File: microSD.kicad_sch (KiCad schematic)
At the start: 7 parts, among them J2 5027740891

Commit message: some cleanup
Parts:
- J2: MnfNumber (none) -> 5027740891
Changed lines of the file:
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@@
       (effects (font (size 1.27 1.27) italic) hide)
+    )
+    (property "MnfNumber" "5027740891" (at 151.765 76.2 0)
+      (effects (font (size 1.27 1.27)) hide)
     )
     (pin "1")

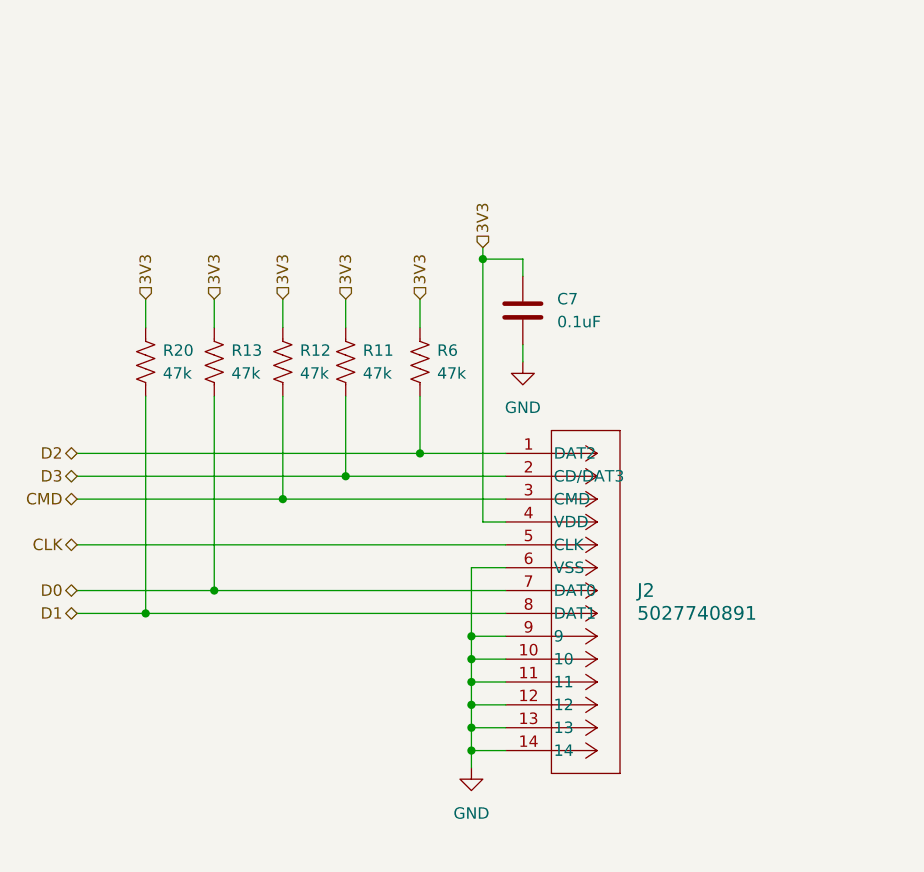
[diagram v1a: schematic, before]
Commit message: updated parts with those available on jlpcb
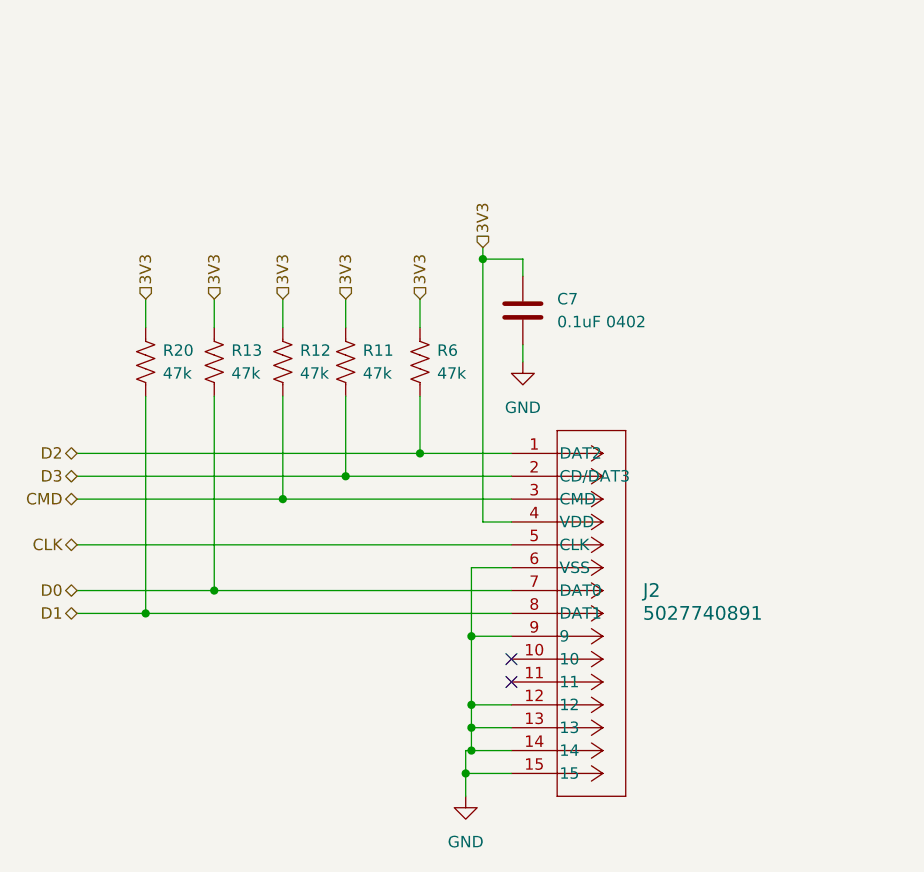
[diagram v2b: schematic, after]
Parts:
- C7: value 0.1uF -> 0.1uF 0402
- J2: footprint microSD:CONN_5027740891_MOL -> microSD2:CONN9_0185-02_GSW
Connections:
- net GND: now also J2.15; no longer J2.10, J2.11
- no-connect marks 0 -> 2
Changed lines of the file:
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@@
 (kicad_sch (version 20230121) (generator eeschema)
   (paper "A4")
-  (junction (at 147.955 101.6) (diameter 0) (color 0 0 0 0)
+  (junction (at 147.32 111.76) (diameter 0) (color 0 0 0 0)
   )
   (junction (at 142.24 76.2) (diameter 0) (color 0 0 0 0)
@@
   (junction (at 147.955 96.52) (diameter 0) (color 0 0 0 0)
   )
-  (junction (at 147.955 99.06) (diameter 0) (color 0 0 0 0)
-  )
+  (no_connect (at 152.4 99.06))
+  (no_connect (at 152.4 101.6))
   (wire (pts (xy 153.67 64.135) (xy 153.67 66.04))
     (stroke (width 0) (type default))
   )
+  (wire (pts (xy 147.32 111.76) (xy 152.4 111.76))
+    (stroke (width 0) (type default))
+  )
   (wire (pts (xy 104.14 76.2) (xy 142.24 76.2))
     (stroke (width 0) (type default))
@@
     (stroke (width 0) (type default))
   )
-  (wire (pts (xy 142.24 76.2) (xy 151.765 76.2))
+  (wire (pts (xy 142.24 76.2) (xy 152.4 76.2))
     (stroke (width 0) (type default))
   )
@@
     (stroke (width 0) (type default))
   )
-  (wire (pts (xy 127 81.28) (xy 151.765 81.28))
+  (wire (pts (xy 127 81.28) (xy 152.4 81.28))
     (stroke (width 0) (type default))
   )
@@
     (stroke (width 0) (type default))
   )
-  (wire (pts (xy 147.955 106.68) (xy 151.765 106.68))
-    (stroke (width 0) (type default))
-  )
-  (wire (pts (xy 147.955 111.125) (xy 147.955 109.22))
-    (stroke (width 0) (type default))
-  )
-  (wire (pts (xy 147.955 109.22) (xy 151.765 109.22))
+  (wire (pts (xy 147.955 106.68) (xy 152.4 106.68))
+    (stroke (width 0) (type default))
+  )
+  (wire (pts (xy 147.32 114.3) (xy 147.32 111.76))
+    (stroke (width 0) (type default))
+  )
+  (wire (pts (xy 147.955 109.22) (xy 152.4 109.22))
     (stroke (width 0) (type default))
   )
@@
     (stroke (width 0) (type default))
   )
-  (wire (pts (xy 147.955 101.6) (xy 147.955 99.06))
-    (stroke (width 0) (type default))
-  )
-  (wire (pts (xy 147.955 88.9) (xy 151.765 88.9))
-    (stroke (width 0) (type default))
-  )
-  (wire (pts (xy 133.985 78.74) (xy 151.765 78.74))
+  (wire (pts (xy 147.32 111.76) (xy 147.32 109.22))
+    (stroke (width 0) (type default))
+  )
+  (wire (pts (xy 147.955 88.9) (xy 152.4 88.9))
+    (stroke (width 0) (type default))
+  )
+  (wire (pts (xy 133.985 78.74) (xy 152.4 78.74))
     (stroke (width 0) (type default))
   )
@@
     (stroke (width 0) (type default))
   )
-  (wire (pts (xy 147.955 104.14) (xy 147.955 101.6))
-    (stroke (width 0) (type default))
-  )
   (wire (pts (xy 104.14 93.98) (xy 111.76 93.98))
     (stroke (width 0) (type default))
   )
-  (wire (pts (xy 111.76 93.98) (xy 151.765 93.98))
-    (stroke (width 0) (type default))
-  )
-  (wire (pts (xy 147.955 101.6) (xy 151.765 101.6))
+  (wire (pts (xy 111.76 93.98) (xy 152.4 93.98))
     (stroke (width 0) (type default))
   )
@@
     (stroke (width 0) (type default))
   )
-  (wire (pts (xy 147.955 104.14) (xy 151.765 104.14))
-    (stroke (width 0) (type default))
-  )
-  (wire (pts (xy 149.225 83.82) (xy 151.765 83.82))
+  (wire (pts (xy 147.955 104.14) (xy 152.4 104.14))
+    (stroke (width 0) (type default))
+  )
+  (wire (pts (xy 149.225 83.82) (xy 152.4 83.82))
     (stroke (width 0) (type default))
   )
@@
     (stroke (width 0) (type default))
   )
-  (wire (pts (xy 147.955 96.52) (xy 151.765 96.52))
-    (stroke (width 0) (type default))
-  )
-  (wire (pts (xy 147.955 99.06) (xy 151.765 99.06))
+  (wire (pts (xy 147.955 96.52) (xy 152.4 96.52))
+    (stroke (width 0) (type default))
+  )
+  (wire (pts (xy 147.32 109.22) (xy 147.955 109.22))
     (stroke (width 0) (type default))
   )
@@
     (stroke (width 0) (type default))
   )
-  (wire (pts (xy 119.38 91.44) (xy 151.765 91.44))
+  (wire (pts (xy 119.38 91.44) (xy 152.4 91.44))
     (stroke (width 0) (type default))
   )
@@
     (stroke (width 0) (type default))
   )
-  (wire (pts (xy 104.14 86.36) (xy 151.765 86.36))
+  (wire (pts (xy 104.14 86.36) (xy 152.4 86.36))
     (stroke (width 0) (type default))
   )
@@
     (stroke (width 0) (type default))
   )
-  (wire (pts (xy 147.955 99.06) (xy 147.955 96.52))
+  (wire (pts (xy 147.955 96.52) (xy 147.955 104.14))
     (stroke (width 0) (type default))
   )
@@
       (effects (font (size 1.27 1.27)) (justify left))
     )
-    (property "Value" "0.1uF" (at 157.48 61.595 0)
+    (property "Value" "0.1uF 0402" (at 157.48 61.595 0)
       (effects (font (size 1.27 1.27)) (justify left))
     )
@@
     )
   )
-  (symbol (lib_id "microSD:5027740891") (at 151.765 76.2 0) (unit 1)
-    (in_bom yes) (on_board yes) (dnp no) (fields_autoplaced)
-    (property "Reference" "J2" (at 166.37 91.44 0)
+  (symbol (lib_id "microSD:5027740891") (at 152.4 76.2 0) (unit 1)
+    (in_bom yes) (on_board yes) (dnp no) (fields_autoplaced)
+    (property "Reference" "J2" (at 167.005 91.44 0)
       (effects (font (size 1.524 1.524)) (justify left))
     )
-    (property "Value" "5027740891" (at 166.37 93.98 0)
+    (property "Value" "5027740891" (at 167.005 93.98 0)
       (effects (font (size 1.524 1.524)) (justify left))
     )
-    (property "Footprint" "microSD:CONN_5027740891_MOL" (at 151.765 76.2 0)
+    (property "Footprint" "microSD2:CONN9_0185-02_GSW" (at 152.4 76.2 0)
       (effects (font (size 1.27 1.27) italic) hide)
     )
-    (property "Datasheet" "5027740891" (at 151.765 76.2 0)
+    (property "Datasheet" "5027740891" (at 152.4 76.2 0)
       (effects (font (size 1.27 1.27) italic) hide)
     )
-    (property "MnfNumber" "5027740891" (at 151.765 76.2 0)
+    (property "MnfNumber" "5027740891" (at 152.4 76.2 0)
       (effects (font (size 1.27 1.27)) hide)
     )
@@
     (pin "13")
     (pin "14")
+    (pin "15")
     (pin "2")
     (pin "3")
@@
     )
   )
-  (symbol (lib_id "power:GND") (at 147.955 111.125 0) (unit 1)
-    (in_bom yes) (on_board yes) (dnp no) (fields_autoplaced)
-    (property "Reference" "#PWR017" (at 147.955 117.475 0)
-      (effects (font (size 1.27 1.27)) hide)
-    )
-    (property "Value" "GND" (at 147.955 116.205 0)
+  (symbol (lib_id "power:GND") (at 147.32 114.3 0) (unit 1)
+    (in_bom yes) (on_board yes) (dnp no) (fields_autoplaced)
+    (property "Reference" "#PWR017" (at 147.32 120.65 0)
+      (effects (font (size 1.27 1.27)) hide)
+    )
+    (property "Value" "GND" (at 147.32 119.38 0)
       (effects (font (size 1.27 1.27)))
     )
-    (property "Footprint" "" (at 147.955 111.125 0)
-      (effects (font (size 1.27 1.27)) hide)
-    )
-    (property "Datasheet" "" (at 147.955 111.125 0)
-      (effects (font (size 1.27 1.27)) hide)
-    )
+    (property "Footprint" "" (at 147.32 114.3 0)
+      (effects (font (size 1.27 1.27)) hide)
+    )
+    (property "Datasheet" "" (at 147.32 114.3 0)
+      (effects (font (size 1.27 1.27)) hide)
+    )

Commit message: moving to through hole microSD connector vertical, and through hole daisy seed to cost optimize.  Surface mount daisy seed headers seemed more expensive
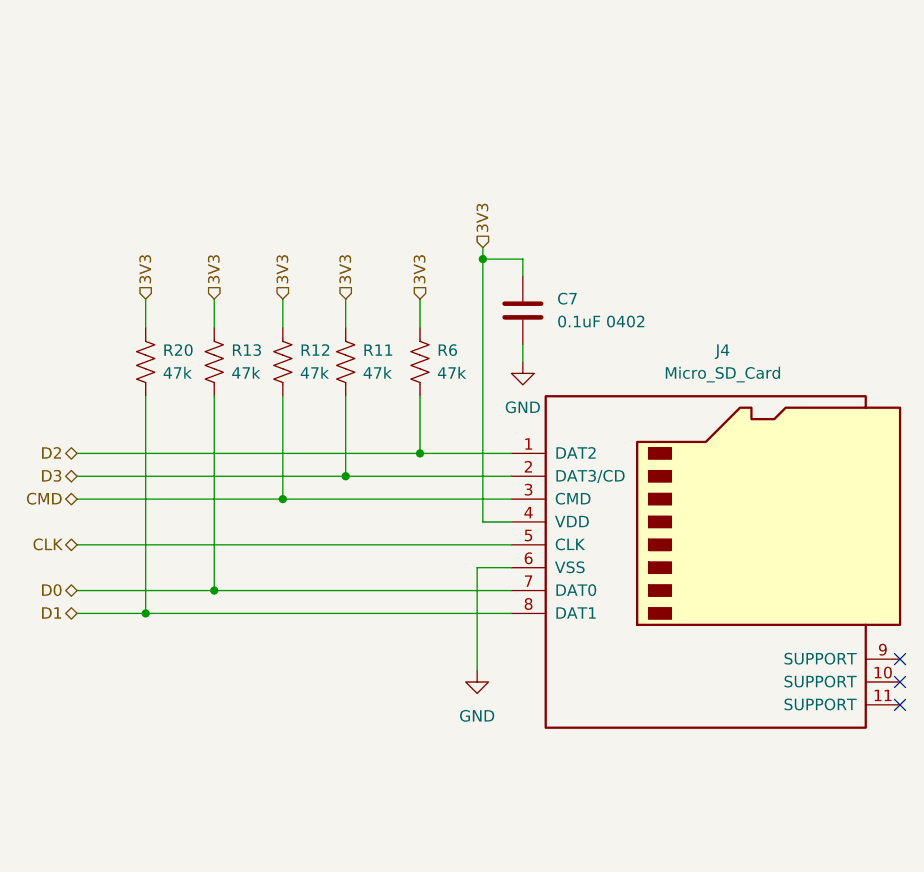
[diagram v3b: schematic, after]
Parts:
- removed J2: 5027740891, microSD2:CONN9_0185-02_GSW, symbol microSD:5027740891
- added J4: Micro_SD_Card, microSDVertical:CONN_PJS008U-3000-0_YAM, symbol microSdVertical:Micro_SD_Card_Vertical
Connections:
- net 3V3: now also J4.4 (VDD)
- net CLK: now also J4.5 (CLK)
- net CMD: now also J4.3 (CMD)
- net D0: now also J4.7 (DAT0)
- net D1: now also J4.8 (DAT1)
- net D2: now also J4.1 (DAT2)
- net D3: now also J4.2 (DAT3/CD)
- net GND: now also J4.6 (VSS)
- no-connect marks 2 -> 3
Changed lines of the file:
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@@
 (kicad_sch (version 20230121) (generator eeschema)
   (paper "A4")
-  (junction (at 147.32 111.76) (diameter 0) (color 0 0 0 0)
-  )
   (junction (at 142.24 76.2) (diameter 0) (color 0 0 0 0)
   )
@@
   (junction (at 133.985 78.74) (diameter 0) (color 0 0 0 0)
   )
-  (junction (at 147.955 106.68) (diameter 0) (color 0 0 0 0)
-  )
-  (junction (at 147.955 104.14) (diameter 0) (color 0 0 0 0)
-  )
   (junction (at 149.225 54.61) (diameter 0) (color 0 0 0 0)
   )
   (junction (at 111.76 93.98) (diameter 0) (color 0 0 0 0)
   )
-  (junction (at 147.955 109.22) (diameter 0) (color 0 0 0 0)
-  )
-  (junction (at 147.955 96.52) (diameter 0) (color 0 0 0 0)
-  )
-  (no_connect (at 152.4 99.06))
-  (no_connect (at 152.4 101.6))
+  (no_connect (at 195.58 104.14))
+  (no_connect (at 195.58 101.6))
+  (no_connect (at 195.58 99.06))
   (wire (pts (xy 153.67 64.135) (xy 153.67 66.04))
     (stroke (width 0) (type default))
   )
-  (wire (pts (xy 147.32 111.76) (xy 152.4 111.76))
-    (stroke (width 0) (type default))
-  )
   (wire (pts (xy 104.14 76.2) (xy 142.24 76.2))
     (stroke (width 0) (type default))
@@
     (stroke (width 0) (type default))
   )
-  (wire (pts (xy 147.955 96.52) (xy 147.955 88.9))
-    (stroke (width 0) (type default))
-  )
   (wire (pts (xy 133.985 69.85) (xy 133.985 78.74))
     (stroke (width 0) (type default))
@@
     (stroke (width 0) (type default))
   )
-  (wire (pts (xy 147.955 106.68) (xy 152.4 106.68))
-    (stroke (width 0) (type default))
-  )
-  (wire (pts (xy 147.32 114.3) (xy 147.32 111.76))
-    (stroke (width 0) (type default))
-  )
-  (wire (pts (xy 147.955 109.22) (xy 152.4 109.22))
+  (wire (pts (xy 148.59 88.9) (xy 148.59 100.33))
     (stroke (width 0) (type default))
   )
@@
     (stroke (width 0) (type default))
   )
-  (wire (pts (xy 147.32 111.76) (xy 147.32 109.22))
-    (stroke (width 0) (type default))
-  )
-  (wire (pts (xy 147.955 88.9) (xy 152.4 88.9))
-    (stroke (width 0) (type default))
-  )
   (wire (pts (xy 133.985 78.74) (xy 152.4 78.74))
     (stroke (width 0) (type default))
@@
     (stroke (width 0) (type default))
   )
-  (wire (pts (xy 147.955 109.22) (xy 147.955 106.68))
+  (wire (pts (xy 148.59 88.9) (xy 152.4 88.9))
     (stroke (width 0) (type default))
   )
@@
     (stroke (width 0) (type default))
   )
-  (wire (pts (xy 147.955 106.68) (xy 147.955 104.14))
-    (stroke (width 0) (type default))
-  )
-  (wire (pts (xy 147.955 104.14) (xy 152.4 104.14))
-    (stroke (width 0) (type default))
-  )
   (wire (pts (xy 149.225 83.82) (xy 152.4 83.82))
     (stroke (width 0) (type default))
@@
     (stroke (width 0) (type default))
   )
-  (wire (pts (xy 147.955 96.52) (xy 152.4 96.52))
-    (stroke (width 0) (type default))
-  )
-  (wire (pts (xy 147.32 109.22) (xy 147.955 109.22))
-    (stroke (width 0) (type default))
-  )
   (wire (pts (xy 149.225 53.34) (xy 149.225 54.61))
     (stroke (width 0) (type default))
@@
     (stroke (width 0) (type default))
   )
-  (wire (pts (xy 147.955 96.52) (xy 147.955 104.14))
-    (stroke (width 0) (type default))
-  )
   (wire (pts (xy 142.24 69.85) (xy 142.24 76.2))
     (stroke (width 0) (type default))
@@
     )
   )
-  (symbol (lib_id "microSD:5027740891") (at 152.4 76.2 0) (unit 1)
-    (in_bom yes) (on_board yes) (dnp no) (fields_autoplaced)
-    (property "Reference" "J2" (at 167.005 91.44 0)
-      (effects (font (size 1.524 1.524)) (justify left))
-    )
-    (property "Value" "5027740891" (at 167.005 93.98 0)
-      (effects (font (size 1.524 1.524)) (justify left))
-    )
-    (property "Footprint" "microSD2:CONN9_0185-02_GSW" (at 152.4 76.2 0)
-      (effects (font (size 1.27 1.27) italic) hide)
-    )
-    (property "Datasheet" "5027740891" (at 152.4 76.2 0)
-      (effects (font (size 1.27 1.27) italic) hide)
-    )
-    (property "MnfNumber" "5027740891" (at 152.4 76.2 0)
+  (symbol (lib_id "Device:R_US") (at 142.24 66.04 0) (unit 1)
+    (in_bom yes) (on_board yes) (dnp no) (fields_autoplaced)
+    (property "Reference" "R6" (at 144.145 64.77 0)
+      (effects (font (size 1.27 1.27)) (justify left))
+    )
+    (property "Value" "47k" (at 144.145 67.31 0)
+      (effects (font (size 1.27 1.27)) (justify left))
+    )
+    (property "Footprint" "Resistor_SMD:R_0402_1005Metric" (at 143.256 66.294 90)
+      (effects (font (size 1.27 1.27)) hide)
+    )
+    (property "Datasheet" "~" (at 142.24 66.04 0)
+      (effects (font (size 1.27 1.27)) hide)
+    )
+    (pin "1")
+    (pin "2")
+    (instances
+      (project "DaisySeedBreakout"
+        (path "/a83c9f4b-f61b-47d4-b39d-4636bff6eb0e"
+          (reference "R6") (unit 1)
+        )
+        (path "/a83c9f4b-f61b-47d4-b39d-4636bff6eb0e/e07e79f0-bef5-432f-b85e-bb16f66114f9"
+          (reference "R14") (unit 1)
+        )
+      )
+    )
+  )
+  (symbol (lib_id "microSdVertical:Micro_SD_Card_Vertical") (at 175.26 83.82 0) (unit 1)
+    (in_bom yes) (on_board yes) (dnp no) (fields_autoplaced)
+    (property "Reference" "J4" (at 175.895 64.77 0)
+      (effects (font (size 1.27 1.27)))
+    )
+    (property "Value" "Micro_SD_Card" (at 175.895 67.31 0)
+      (effects (font (size 1.27 1.27)))
+    )
+    (property "Footprint" "microSDVertical:CONN_PJS008U-3000-0_YAM" (at 204.47 76.2 0)
+      (effects (font (size 1.27 1.27)) hide)
+    )
+    (property "Datasheet" "http://katalog.we-online.de/em/datasheet/693072010801.pdf" (at 175.26 83.82 0)
       (effects (font (size 1.27 1.27)) hide)
     )
@@
     (pin "10")
     (pin "11")
-    (pin "12")
-    (pin "13")
-    (pin "14")
-    (pin "15")
     (pin "2")
     (pin "3")
@@
     (instances
       (project "DaisySeedBreakout"
-        (path "/a83c9f4b-f61b-47d4-b39d-4636bff6eb0e"
-          (reference "J2") (unit 1)
-        )
         (path "/a83c9f4b-f61b-47d4-b39d-4636bff6eb0e/e07e79f0-bef5-432f-b85e-bb16f66114f9"
           (reference "J4") (unit 1)
@@
     )
   )
-  (symbol (lib_id "Device:R_US") (at 142.24 66.04 0) (unit 1)
-    (in_bom yes) (on_board yes) (dnp no) (fields_autoplaced)
-    (property "Reference" "R6" (at 144.145 64.77 0)
-      (effects (font (size 1.27 1.27)) (justify left))
-    )
-    (property "Value" "47k" (at 144.145 67.31 0)
-      (effects (font (size 1.27 1.27)) (justify left))
-    )
-    (property "Footprint" "Resistor_SMD:R_0402_1005Metric" (at 143.256 66.294 90)
-      (effects (font (size 1.27 1.27)) hide)
-    )
-    (property "Datasheet" "~" (at 142.24 66.04 0)
-      (effects (font (size 1.27 1.27)) hide)
-    )
-    (pin "1")
-    (pin "2")
-    (instances
-      (project "DaisySeedBreakout"
-        (path "/a83c9f4b-f61b-47d4-b39d-4636bff6eb0e"
-          (reference "R6") (unit 1)
-        )
-        (path "/a83c9f4b-f61b-47d4-b39d-4636bff6eb0e/e07e79f0-bef5-432f-b85e-bb16f66114f9"
-          (reference "R14") (unit 1)
-        )
-      )
-    )
-  )
   (symbol (lib_id "Device:R_US") (at 133.985 66.04 0) (unit 1)
     (in_bom yes) (on_board yes) (dnp no) (fields_autoplaced)
@@
     )
   )
-  (symbol (lib_id "power:GND") (at 147.32 114.3 0) (unit 1)
-    (in_bom yes) (on_board yes) (dnp no) (fields_autoplaced)
-    (property "Reference" "#PWR017" (at 147.32 120.65 0)
-      (effects (font (size 1.27 1.27)) hide)
-    )
-    (property "Value" "GND" (at 147.32 119.38 0)
+  (symbol (lib_id "power:GND") (at 148.59 100.33 0) (unit 1)
+    (in_bom yes) (on_board yes) (dnp no) (fields_autoplaced)
+    (property "Reference" "#PWR017" (at 148.59 106.68 0)
+      (effects (font (size 1.27 1.27)) hide)
+    )
+    (property "Value" "GND" (at 148.59 105.41 0)
       (effects (font (size 1.27 1.27)))
     )
-    (property "Footprint" "" (at 147.32 114.3 0)
-      (effects (font (size 1.27 1.27)) hide)
-    )
-    (property "Datasheet" "" (at 147.32 114.3 0)
-      (effects (font (size 1.27 1.27)) hide)
-    )
+    (property "Footprint" "" (at 148.59 100.33 0)
+      (effects (font (size 1.27 1.27)) hide)
+    )
+    (property "Datasheet" "" (at 148.59 100.33 0)
+      (effects (font (size 1.27 1.27)) hide)
+    )

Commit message: Moved everything to the top side
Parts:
- C7: footprint Capacitor_SMD:C_0402_1005Metric -> Capacitor_SMD:C_0603_1608Metric
- R11, R12, R13, R20, R6: footprint Resistor_SMD:R_0402_1005Metric -> Resistor_SMD:R_0603_1608Metric
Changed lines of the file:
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@@
       (effects (font (size 1.27 1.27)) (justify left))
     )
-    (property "Footprint" "Capacitor_SMD:C_0402_1005Metric" (at 154.6352 64.135 0)
+    (property "Footprint" "Capacitor_SMD:C_0603_1608Metric" (at 154.6352 64.135 0)
       (effects (font (size 1.27 1.27)) hide)
     )
@@
       (effects (font (size 1.27 1.27)) (justify left))
     )
-    (property "Footprint" "Resistor_SMD:R_0402_1005Metric" (at 112.776 66.294 90)
+    (property "Footprint" "Resistor_SMD:R_0603_1608Metric" (at 112.776 66.294 90)
       (effects (font (size 1.27 1.27)) hide)
     )
@@
       (effects (font (size 1.27 1.27)) (justify left))
     )
-    (property "Footprint" "Resistor_SMD:R_0402_1005Metric" (at 143.256 66.294 90)
+    (property "Footprint" "Resistor_SMD:R_0603_1608Metric" (at 143.256 66.294 90)
       (effects (font (size 1.27 1.27)) hide)
     )
@@
       (effects (font (size 1.27 1.27)) (justify left))
     )
-    (property "Footprint" "Resistor_SMD:R_0402_1005Metric" (at 135.001 66.294 90)
+    (property "Footprint" "Resistor_SMD:R_0603_1608Metric" (at 135.001 66.294 90)
       (effects (font (size 1.27 1.27)) hide)
     )
@@
       (effects (font (size 1.27 1.27)) (justify left))
     )
-    (property "Footprint" "Resistor_SMD:R_0402_1005Metric" (at 128.016 66.294 90)
+    (property "Footprint" "Resistor_SMD:R_0603_1608Metric" (at 128.016 66.294 90)
       (effects (font (size 1.27 1.27)) hide)
     )
@@
       (effects (font (size 1.27 1.27)) (justify left))
     )
-    (property "Footprint" "Resistor_SMD:R_0402_1005Metric" (at 120.396 66.294 90)
+    (property "Footprint" "Resistor_SMD:R_0603_1608Metric" (at 120.396 66.294 90)
       (effects (font (size 1.27 1.27)) hide)
     )
